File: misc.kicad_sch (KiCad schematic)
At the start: 126 parts, among them CN2 Expansion, CN3 Cartridge, CN5 1P, CN504 AV Out, CN6 1P, IC401 74ACT241, IC513 MC34063AM, IC514 L7805, IC701 PIC16F630/18324, IC901 TL974, J1 Barrel_Jack, J2 EXT, Q1 MMBT3904, U1 TPS564257DRLR, U4 L7805

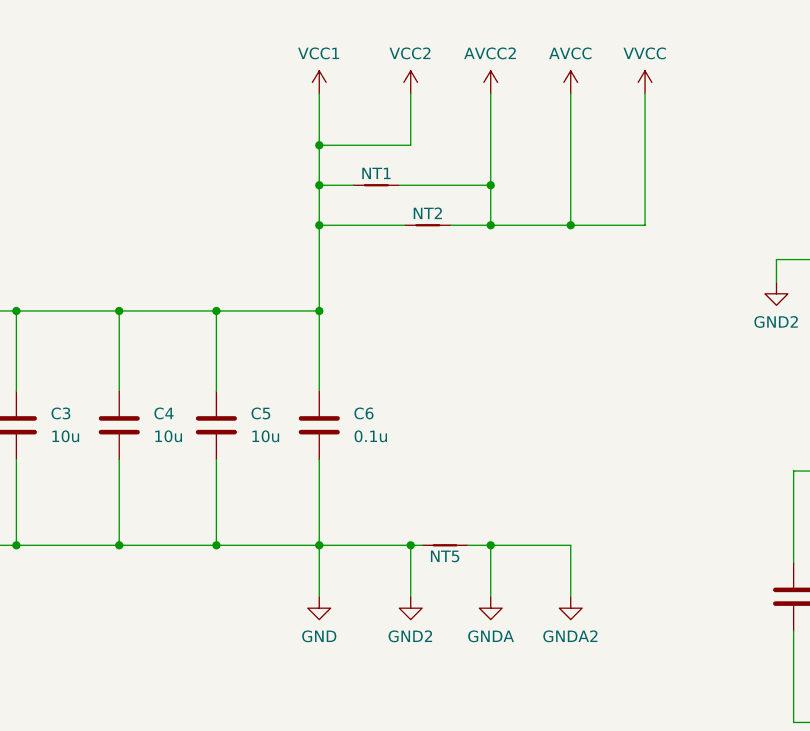
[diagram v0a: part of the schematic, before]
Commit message: Review/add 32X bodges.
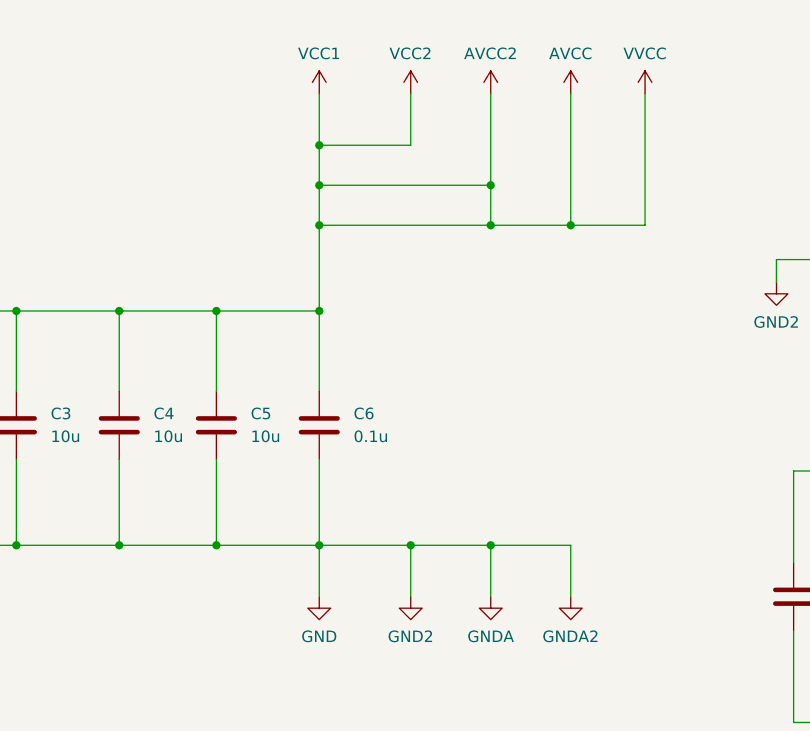
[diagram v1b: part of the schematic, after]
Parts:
- removed NT1, NT2, NT5: ~, NetTie:NetTie-2_SMD_Pad0.5mm, symbol Device:NetTie_2
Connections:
- net GNDA is gone; now on net GND: CN504.10 (Pin_10)
- net VCC1 is gone; now on net AVCC: C1.1, C1.1, C2.1, C3.1, C4.1, C401.1, C45.1, C5.1, C584.1, C6.1, C701.1, CE17.1, CE18.1, CE19.1, CE27.1, CE28.1, CE508.1, CE509.1, CE517.1, CE518.1, CN2.a26 (Pin_a26), CN2.b26 (Pin_b26), CN3.a2 (Pin_a2), CN3.a31 (Pin_a31), D1.1 (K), EM15.3, EM25.3, IC401.20 (VCC), IC514.1 (IN), IC701.1 (VDD), J2.1 (Pin_1), L1.2, L507.1, L6.2, NF502.3, OSC1.14 (Vcc), R3.1, R5.2, R553.1, R556.1, R601.1, R65.1, U4.3 (OUT)
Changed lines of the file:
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@@
     (stroke (width 0) (type default))
   )
-  (wire (pts (xy 226.06 210.82) (xy 230.505 210.82))
-    (stroke (width 0) (type default))
-  )
   (wire (pts (xy 161.925 40.64) (xy 177.165 40.64))
     (stroke (width 0) (type default))
@@
     (stroke (width 0) (type default))
   )
-  (wire (pts (xy 211.455 210.82) (xy 220.98 210.82))
-    (stroke (width 0) (type default))
-  )
   (wire (pts (xy 32.385 220.345) (xy 36.83 220.345))
     (stroke (width 0) (type default))
@@
     (stroke (width 0) (type default))
   )
+  (wire (pts (xy 211.455 206.375) (xy 230.505 206.375))
+    (stroke (width 0) (type default))
+  )
   (bus (pts (xy 207.645 38.1) (xy 207.645 24.13))
     (stroke (width 0) (type default))
@@
     (stroke (width 0) (type default))
   )
-  (wire (pts (xy 211.455 206.375) (xy 215.265 206.375))
-    (stroke (width 0) (type default))
-  )
   (wire (pts (xy 572.135 184.785) (xy 567.69 184.785))
     (stroke (width 0) (type default))
   )
-  (wire (pts (xy 220.345 206.375) (xy 230.505 206.375))
-    (stroke (width 0) (type default))
-  )
   (wire (pts (xy 504.19 95.885) (xy 504.19 90.805))
     (stroke (width 0) (type default))
@@
     (stroke (width 0) (type default))
   )
-  (wire (pts (xy 227.965 246.38) (xy 230.505 246.38))
-    (stroke (width 0) (type default))
-  )
   (wire (pts (xy 572.135 172.72) (xy 572.135 184.785))
     (stroke (width 0) (type default))
@@
     (stroke (width 0) (type default))
   )
+  (wire (pts (xy 211.455 210.82) (xy 230.505 210.82))
+    (stroke (width 0) (type default))
+  )
   (wire (pts (xy 605.155 139.065) (xy 592.455 139.065))
     (stroke (width 0) (type default))
@@
     (stroke (width 0) (type default))
   )
-  (wire (pts (xy 221.615 246.38) (xy 222.885 246.38))
+  (wire (pts (xy 221.615 246.38) (xy 230.505 246.38))
     (stroke (width 0) (type default))
   )
@@
     )
   )
-  (symbol (lib_id "Device:NetTie_2") (at 223.52 210.82 0) (unit 1)
-    (in_bom no) (on_board yes) (dnp no)
-    (property "Reference" "NT2" (at 223.52 209.55 0)
-      (effects (font (size 1.27 1.27)))
-    )
-    (property "Value" "~" (at 223.52 208.28 0)
-      (effects (font (size 1.27 1.27)))
-    )
-    (property "Footprint" "NetTie:NetTie-2_SMD_Pad0.5mm" (at 223.52 210.82 0)
-      (effects (font (size 1.27 1.27)) hide)
-    )
-    (property "Datasheet" "~" (at 223.52 210.82 0)
-      (effects (font (size 1.27 1.27)) hide)
-    )
-    (pin "1")
-    (pin "2")
-    (instances
-      (project "Neptune"
-        (path "/bcc23b51-b742-4ae5-9dd6-d96a24058944/01513199-62c5-4123-a151-ccd381a5e6c1"
-          (reference "NT2") (unit 1)
-        )
-      )
-    )
-  )
   (symbol (lib_id "Device:C") (at 47.625 227.965 0) (unit 1)
     (in_bom yes) (on_board yes) (dnp no)
@@
     )
   )
-  (symbol (lib_id "Device:NetTie_2") (at 217.805 206.375 0) (unit 1)
-    (in_bom no) (on_board yes) (dnp no)
-    (property "Reference" "NT1" (at 217.805 205.105 0)
-      (effects (font (size 1.27 1.27)))
-    )
-    (property "Value" "~" (at 217.805 203.835 0)
-      (effects (font (size 1.27 1.27)))
-    )
-    (property "Footprint" "NetTie:NetTie-2_SMD_Pad0.5mm" (at 217.805 206.375 0)
-      (effects (font (size 1.27 1.27)) hide)
-    )
-    (property "Datasheet" "~" (at 217.805 206.375 0)
-      (effects (font (size 1.27 1.27)) hide)
-    )
-    (pin "1")
-    (pin "2")
-    (instances
-      (project "Neptune"
-        (path "/bcc23b51-b742-4ae5-9dd6-d96a24058944/01513199-62c5-4123-a151-ccd381a5e6c1"
-          (reference "NT1") (unit 1)
-        )
-      )
-    )
-  )
   (symbol (lib_id "power:GND") (at 77.47 180.975 0) (unit 1)
     (in_bom yes) (on_board yes) (dnp no) (fields_autoplaced)
@@
         )
       )
-    )
-  )
-  (symbol (lib_id "Device:NetTie_2") (at 225.425 246.38 0) (mirror x) (unit 1)
-    (in_bom no) (on_board yes) (dnp no)
-    (property "Reference" "NT5" (at 225.425 247.65 0)
-      (effects (font (size 1.27 1.27)))
-    )
-    (property "Value" "~" (at 225.425 248.92 0)
-      (effects (font (size 1.27 1.27)))
-    )
-    (property "Footprint" "NetTie:NetTie-2_SMD_Pad0.5mm" (at 225.425 246.38 0)
-      (effects (font (size 1.27 1.27)) hide)
-    )
-    (property "Datasheet" "~" (at 225.425 246.38 0)
-      (effects (font (size 1.27 1.27)) hide)
-    )
-    (pin "1")
-    (pin "2")
-    (instances
-      (project "Neptune"
-        (path "/bcc23b51-b742-4ae5-9dd6-d96a24058944/01513199-62c5-4123-a151-ccd381a5e6c1"
-          (reference "NT5") (unit 1)
-        )
-      )

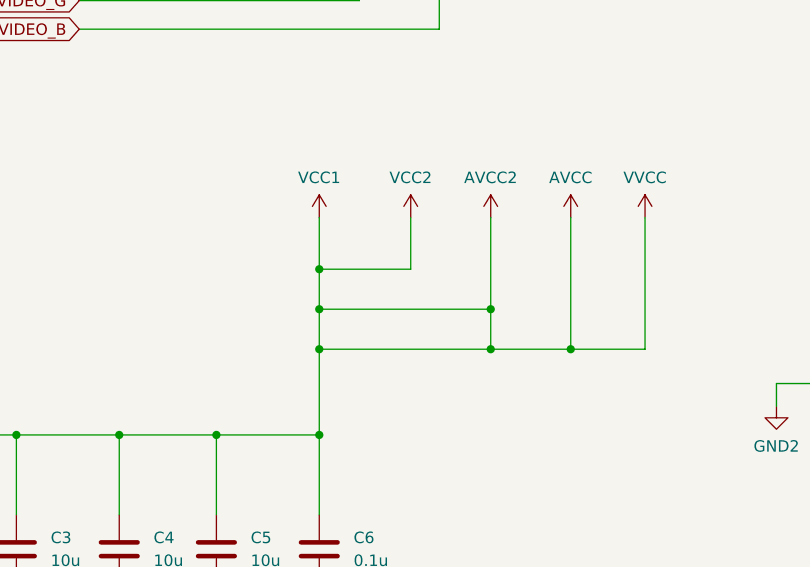
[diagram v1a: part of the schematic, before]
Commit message: Add missing/extra decoupling on 32X side.
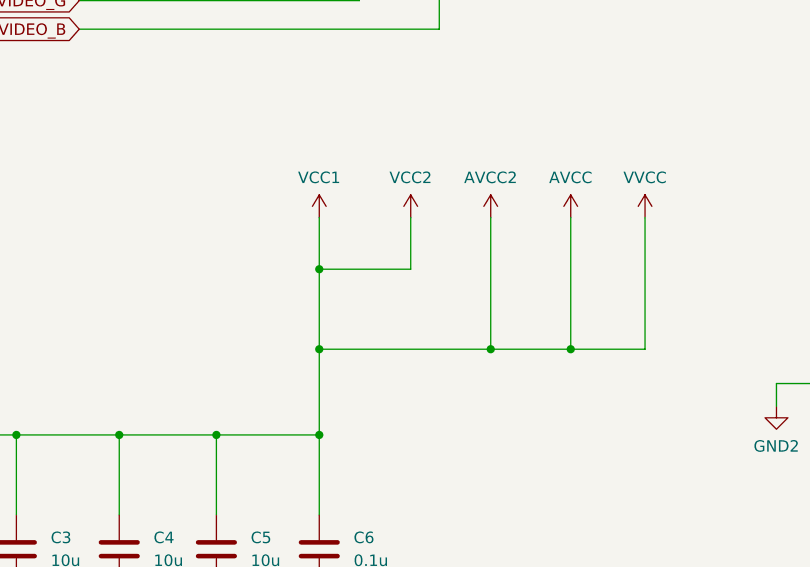
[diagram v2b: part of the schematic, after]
